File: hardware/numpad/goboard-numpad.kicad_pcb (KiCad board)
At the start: 2 copper layers, 74.9 x 104.1 mm, 45 parts, among them J1 Conn_02x05_Top_Bottom, J2 Conn_01x01, J3 Conn_01x05, J4 Conn_01x02_Female, J5 Conn_01x02_Male, SW1 SW_Push, SW10 5, SW12 2, SW13 dot, SW14 times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

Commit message: Numpad: Exchange footprint of the numpad-LED connection
The 2.54 mm pin-header did not fit between the switches as the
silkscreens overlapped.
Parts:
- J4, J5: footprint Connector_PinHeader_2.54mm:PinHeader_1x02_P2.54mm_Vertical -> Connector_PinSocket_2.00mm:PinSocket_1x02_P2.00mm_Vertical
- moved J5 0.34 mm to (117.8, 53.0)
- moved J4 0.08 mm to (143.7, 62.0)

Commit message: Numpad: Exchange the debug-conn footprint for one without silkscreen
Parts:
- J1: footprint footprints:programming_port_st_link_clone -> footprints:programming_port_st_link_clone_without_silkscreen_outline
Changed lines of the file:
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@@
     )
   )
-  (footprint "footprints:programming_port_st_link_clone" (layer "F.Cu")
+  (footprint "footprints:programming_port_st_link_clone_without_silkscreen_outline" (layer "F.Cu")
     (at 122.33 115.225 -90)
     (descr "Through hole straight pin header, 2x05, 2.54mm pitch, double rows")
@@
     (property "Sheetname" "")
     (attr through_hole)
-    (fp_text reference "J1" (at -2.225 -3.77 180) (layer "F.SilkS")
+    (fp_text reference "J1" (at 4.99 -6.47 90) (layer "F.SilkS")
       (effects (font (size 1 1) (thickness 0.15)))
     )
-    (fp_text value "Conn_02x05_Top_Bottom" (at 5.04 4.02 -270) (layer "F.Fab")
+    (fp_text value "Conn_02x05_Top_Bottom" (at 5.04 4.02 -90) (layer "F.Fab")
       (effects (font (size 1 1) (thickness 0.15)))
     )
-    (fp_text user "${REFERENCE}" (at 5.08 -1.27 -90) (layer "F.Fab")
+    (fp_text user "${REFERENCE}" (at 5.08 -1.27 90) (layer "F.Fab")
       (effects (font (size 1 1) (thickness 0.15)))
     )
-    (fp_line (start -4.92 -5.77) (end -4.92 -2.1) (layer "F.SilkS") (width 0.12))
-    (fp_line (start 2.83 3.23) (end 2.83 2.23) (layer "F.SilkS") (width 0.12))
-    (fp_line (start -4.92 -5.77) (end 15.08 -5.77) (layer "F.SilkS") (width 0.12))
-    (fp_line (start 15.08 -5.77) (end 15.08 -2.1) (layer "F.SilkS") (width 0.12))
+    (fp_line (start -1.33 1.33) (end -1.33 0) (layer "F.SilkS") (width 0.12))
     (fp_line (start 0 1.33) (end -1.33 1.33) (layer "F.SilkS") (width 0.12))
-    (fp_line (start 7.33 2.23) (end 7.33 3.23) (layer "F.SilkS") (width 0.12))
-    (fp_line (start 2.83 2.23) (end 7.33 2.23) (layer "F.SilkS") (width 0.12))
-    (fp_line (start -4.92 3.23) (end -4.92 -0.4) (layer "F.SilkS") (width 0.12))
-    (fp_line (start 15.08 3.23) (end -4.92 3.23) (layer "F.SilkS") (width 0.12))
-    (fp_line (start 15.08 -0.4) (end 15.08 3.23) (layer "F.SilkS") (width 0.12))
-    (fp_line (start -1.33 1.33) (end -1.33 0) (layer "F.SilkS") (width 0.12))
+    (fp_line (start 16.65 -0.05) (end 16.65 -2.6) (layer "F.CrtYd") (width 0.05))
+    (fp_line (start -5.37 0.05) (end -5.37 1.5) (layer "F.CrtYd") (width 0.05))
+    (fp_line (start -5.37 -2.5) (end -6.5 -2.5) (layer "F.CrtYd") (width 0.05))
+    (fp_line (start -6.5 0.05) (end -5.37 0.05) (layer "F.CrtYd") (width 0.05))
+    (fp_line (start 15.53 1.5) (end 15.53 -0.05) (layer "F.CrtYd") (width 0.05))
     (fp_line (start 16.65 -2.6) (end 15.53 -2.6) (layer "F.CrtYd") (width 0.05))
-    (fp_line (start 16.65 -0.05) (end 16.65 -2.6) (layer "F.CrtYd") (width 0.05))
-    (fp_line (start -5.37 -6.27) (end -5.37 -2.5) (layer "F.CrtYd") (width 0.05))
+    (fp_line (start -5.37 1.5) (end 15.53 1.5) (layer "F.CrtYd") (width 0.05))
+    (fp_line (start 15.53 -4) (end -5.37 -4) (layer "F.CrtYd") (width 0.05))
+    (fp_line (start 15.53 -2.6) (end 15.53 -4) (layer "F.CrtYd") (width 0.05))
+    (fp_line (start -6.5 -2.5) (end -6.5 0.05) (layer "F.CrtYd") (width 0.05))
+    (fp_line (start -5.37 -4) (end -5.37 -2.5) (layer "F.CrtYd") (width 0.05))
     (fp_line (start 15.53 -0.05) (end 16.65 -0.05) (layer "F.CrtYd") (width 0.05))
-    (fp_line (start 15.53 3.73) (end 15.53 -0.05) (layer "F.CrtYd") (width 0.05))
-    (fp_line (start -5.37 3.73) (end 15.53 3.73) (layer "F.CrtYd") (width 0.05))
-    (fp_line (start -6.5 0.05) (end -5.37 0.05) (layer "F.CrtYd") (width 0.05))
-    (fp_line (start -5.37 0.05) (end -5.37 3.73) (layer "F.CrtYd") (width 0.05))
-    (fp_line (start -6.5 -2.5) (end -6.5 0.05) (layer "F.CrtYd") (width 0.05))
-    (fp_line (start 15.53 -6.27) (end -5.37 -6.27) (layer "F.CrtYd") (width 0.05))
-    (fp_line (start -5.37 -2.5) (end -6.5 -2.5) (layer "F.CrtYd") (width 0.05))
-    (fp_line (start 15.53 -2.6) (end 15.53 -6.27) (layer "F.CrtYd") (width 0.05))
-    (pad "" np_thru_hole oval (at -2.67 -1.27) (size 1 2.5) (drill oval 1 2.5) (layers F&B.Cu *.Mask))
     (pad "" smd rect (at 15.16 -1.27 180) (size 1 2) (layers "B.Cu" "B.Paste" "B.Mask"))
-    (pad "" np_thru_hole oval (at 12.83 -1.27 180) (size 1 2.5) (drill oval 1 2.5) (layers F&B.Cu *.Mask))
+    (pad "" smd rect (at -5 -1.27) (size 1 2) (layers "B.Cu" "B.Paste" "B.Mask"))
     (pad "" smd rect (at -5 -1.27 180) (size 1 2) (layers "F.Cu" "F.Paste" "F.Mask"))
-    (pad "" smd rect (at -5 -1.27) (size 1 2) (layers "B.Cu" "B.Paste" "B.Mask"))
+    (pad "" np_thru_hole oval (at 12.58 -1.27 180) (size 1 3) (drill oval 1 3) (layers F&B.Cu *.Mask))
+    (pad "" np_thru_hole oval (at -2.42 -1.27) (size 1 3) (drill oval 1 3) (layers F&B.Cu *.Mask))
     (pad "" smd rect (at 15.16 -1.27 180) (size 1 2) (layers "F.Cu" "F.Paste" "F.Mask"))
     (pad "1" thru_hole rect (at 0 0) (size 1.7 1.7) (drill 1) (layers *.Cu *.Mask)

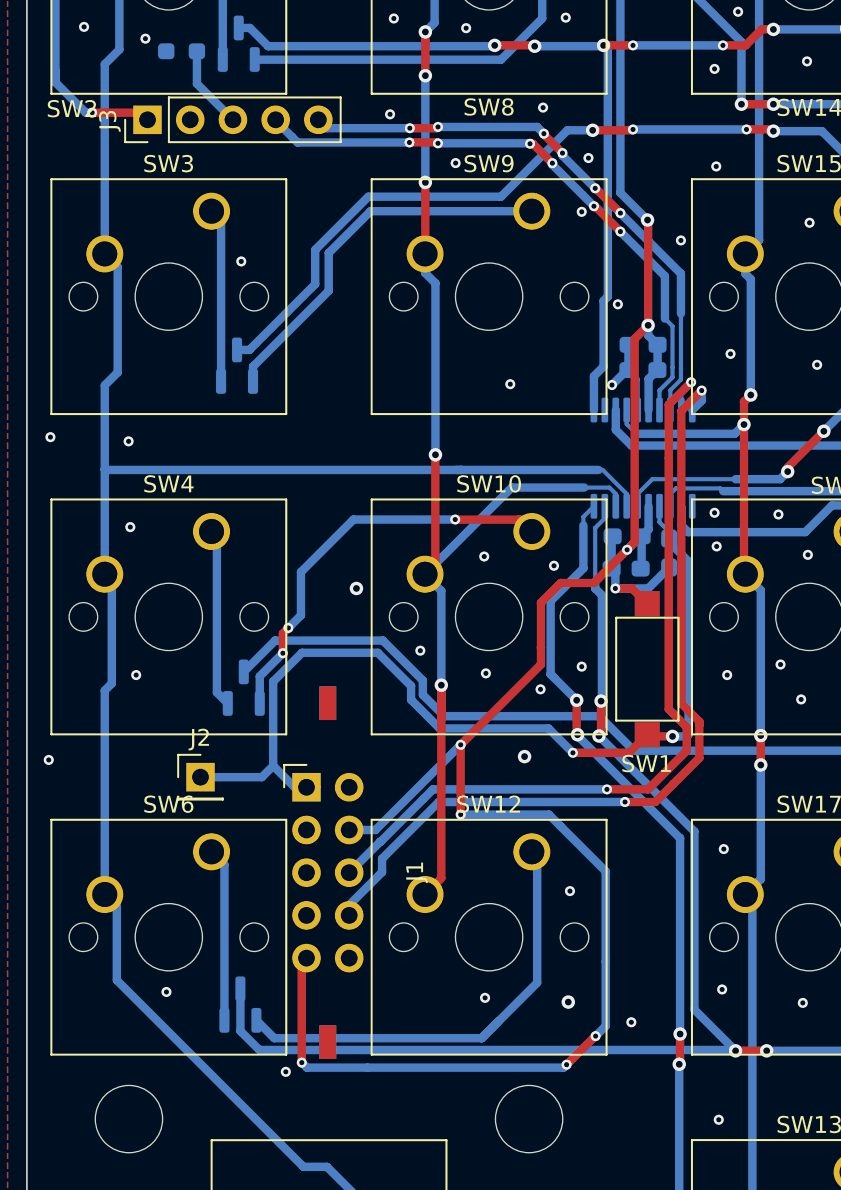
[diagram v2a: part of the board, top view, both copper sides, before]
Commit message: Numpad: Configure designrules for JLCPCB + Fix Errors
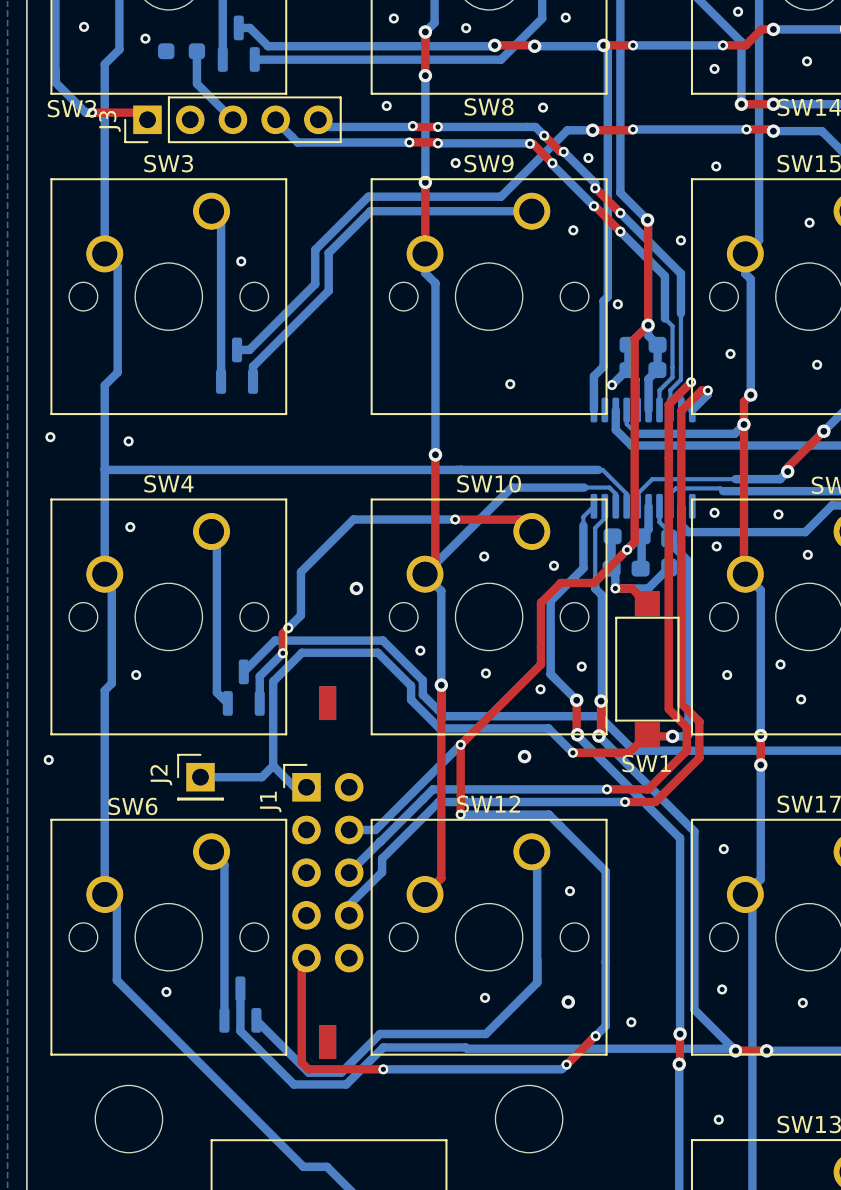
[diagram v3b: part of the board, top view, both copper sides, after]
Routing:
- net /Keys/ROW_3: track 80.2 -> 82.0 mm
- net Net-(D5-Pad1): track 27.9 -> 29.5 mm
- net /SWDCLK: track 49.7 -> 50.2 mm
- net GND: vias 87 -> 86

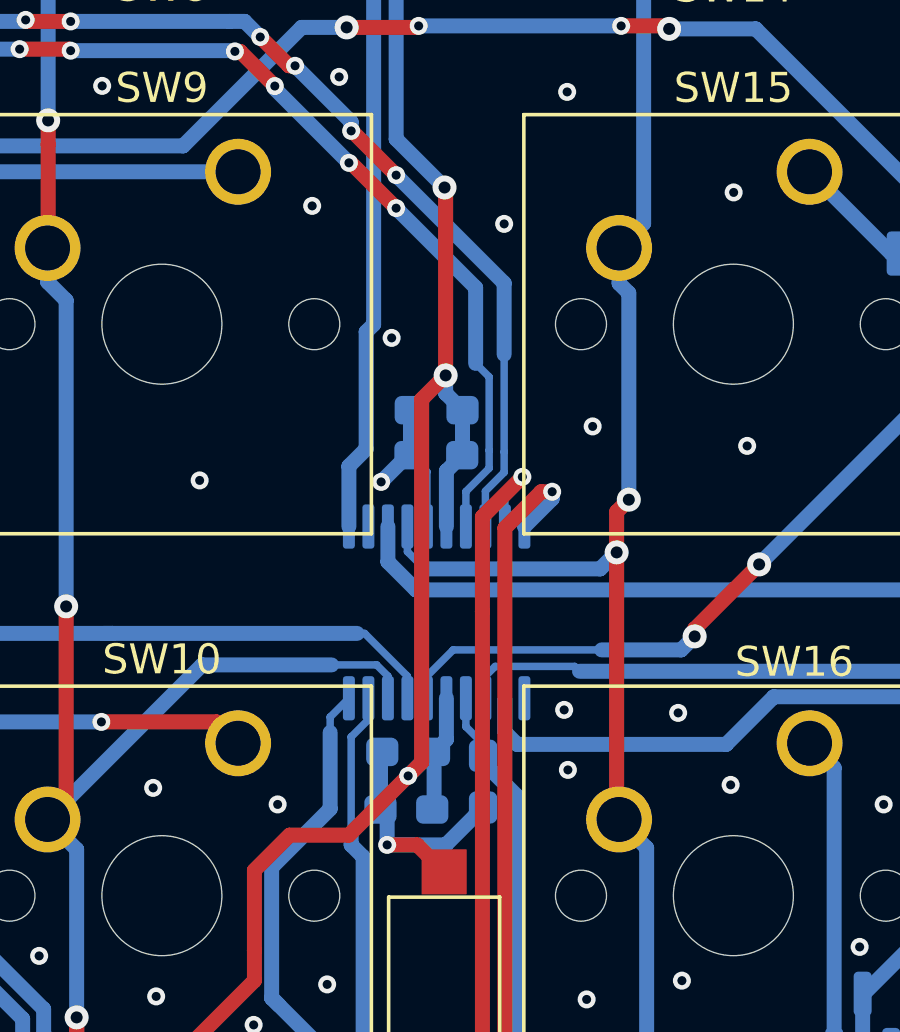
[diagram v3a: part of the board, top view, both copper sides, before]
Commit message: Numpad: Update PCB
The footprint of two capacitors were changed.
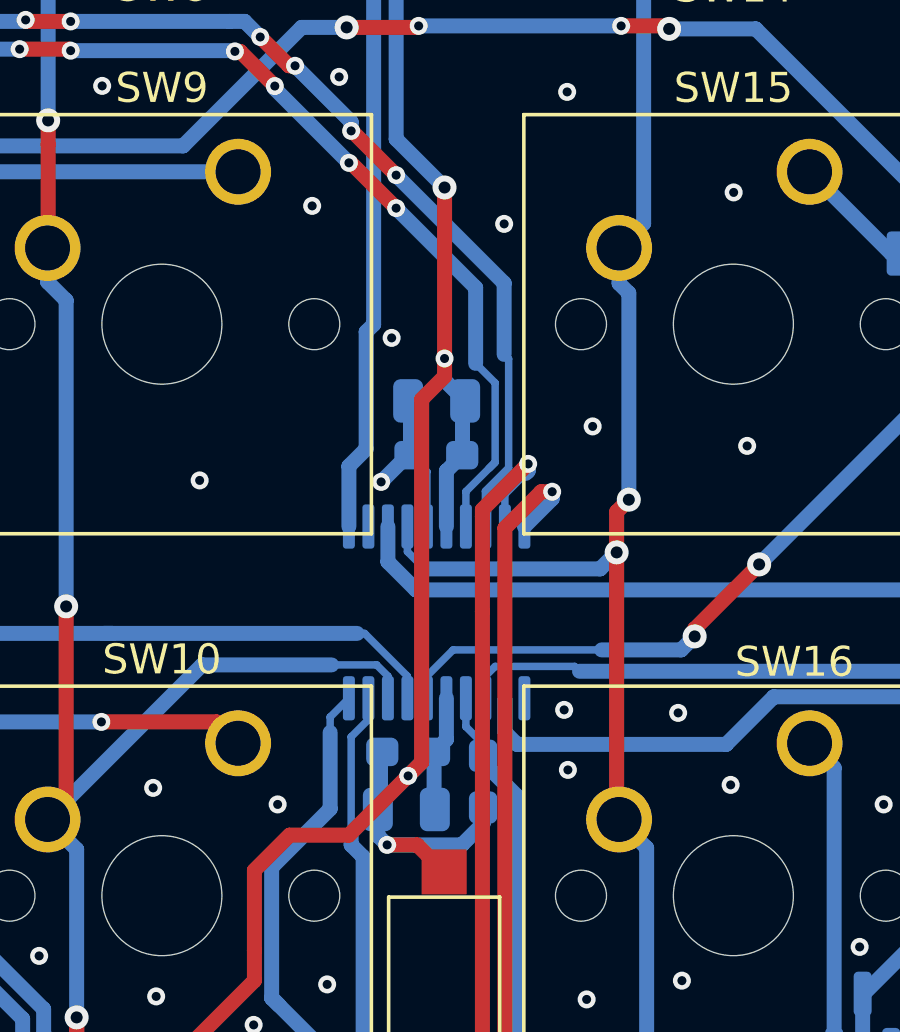
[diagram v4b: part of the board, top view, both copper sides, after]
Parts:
- C3, C5: footprint Capacitor_SMD:C_0603_1608Metric_Pad1.08x0.95mm_HandSolder -> Capacitor_SMD:C_0805_2012Metric
- moved C3 0.31 mm to (142.3, 88.6)
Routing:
- net /SWDIO: track 47.9 -> 48.8 mm

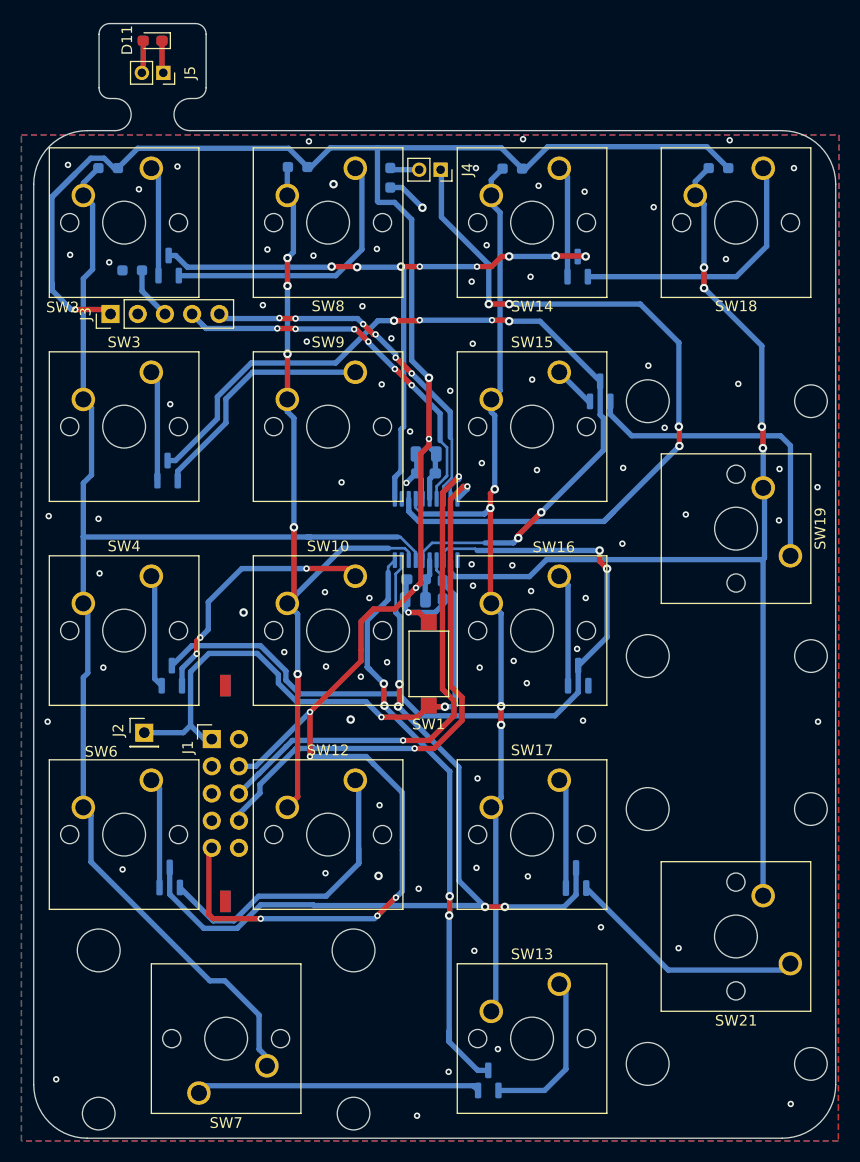
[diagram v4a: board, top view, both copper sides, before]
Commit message: Numpad: Connect the break-away-board to the main with traces
This allows software development without having to solder the LED to the
PCB with wires.
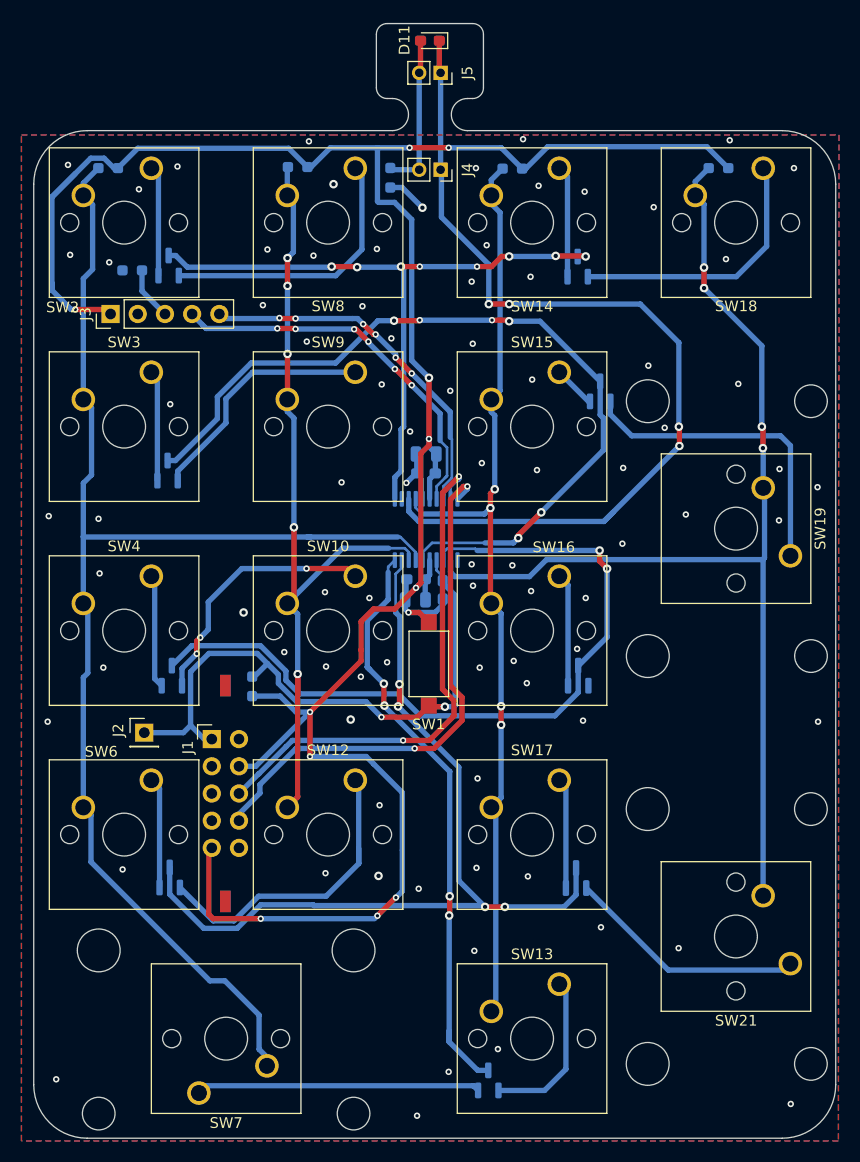
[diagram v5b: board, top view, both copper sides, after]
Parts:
- added R2: 10k, Resistor_SMD:R_0603_1608Metric_Pad0.98x0.95mm_HandSolder, B.Cu at (126.1, 110.3)
- moved D11 25.9 mm to (142.7, 50.0)
- moved J5 25.9 mm to (143.7, 53.0)
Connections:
- D11 pad 1: Net-(D11-Pad1) -> /mcu/LED_NUMLOCK
- D11 pad 2: Net-(D11-Pad2) -> Net-(J4-Pad2)
- J5 pad 1: Net-(D11-Pad1) -> /mcu/LED_NUMLOCK
- J5 pad 2: Net-(D11-Pad2) -> Net-(J4-Pad2)
- U1 pad 1: unconnected-(U1-Pad1) -> GND
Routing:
- net /mcu/LED_NUMLOCK: track 74.3 -> 86.4 mm
- net Net-(J4-Pad2): track 2.30 -> 14.4 mm
- net VCC: track 218.7 -> 224.7 mm, vias 9 -> 11
- net Net-(D11-Pad2): track 3.05 -> 0.00 mm
- net Net-(D11-Pad1): track 3.05 -> 0.00 mm
- net /RESET: track 56.1 -> 58.1 mm
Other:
- outline, holes or cut-outs redrawn
